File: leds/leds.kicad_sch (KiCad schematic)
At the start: 0 parts

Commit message: first draft
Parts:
- added H1, H2, H3, H4: MountingHole_Pad, MountingHole:MountingHole_4mm_Pad_Via, symbol Mechanical:MountingHole_Pad
- added H5, H6, H7, H8: MountingHole_Pad, MountingHole:MountingHole_3.2mm_M3_Pad_Via, symbol Mechanical:MountingHole_Pad
- added TP10, TP11, TP12, TP13, TP14, TP15, TP16, TP5, TP6, TP7, TP8, TP9: LabeledTestPoint, easyeda2kicad:LabeledTestPoint, symbol easyeda2kicad:LabeledTestPoint
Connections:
- net buckconverter/VIN: now also H1.1, H2.1
- new net GND: H3.1, H4.1, H5.1, H6.1, H7.1, H8.1
- new net a2d/AIN1: TP13.1
- new net a2d/AIN2: TP14.1
- new net a2d/AIN3: TP15.1
- new net a2d/AIN4: TP16.1
- new net esp32/EN1: TP9.1
- new net esp32/EN2: TP10.1
- new net esp32/EN3: TP11.1
- new net esp32/EN4: TP12.1
- new net esp32/LED1: TP5.1
- new net esp32/LED2: TP6.1
- new net esp32/LED3: TP7.1
- new net esp32/LED4: TP8.1
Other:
- added sheet a2d (a2d.kicad_sch)
- added sheet led_channel2 (led_channel.kicad_sch)
- added sheet led_channel3 (led_channel.kicad_sch)
- sheet esp32 ports: added EN1, EN2, EN3, EN4, LED1, LED2, LED3, LED4; removed none
- sheet led_channel ports: added 12V, DEN, DIN, IN, IS; removed none
- sheet led_channel1 ports: added 12V, DEN, DIN, IN, IS; removed none

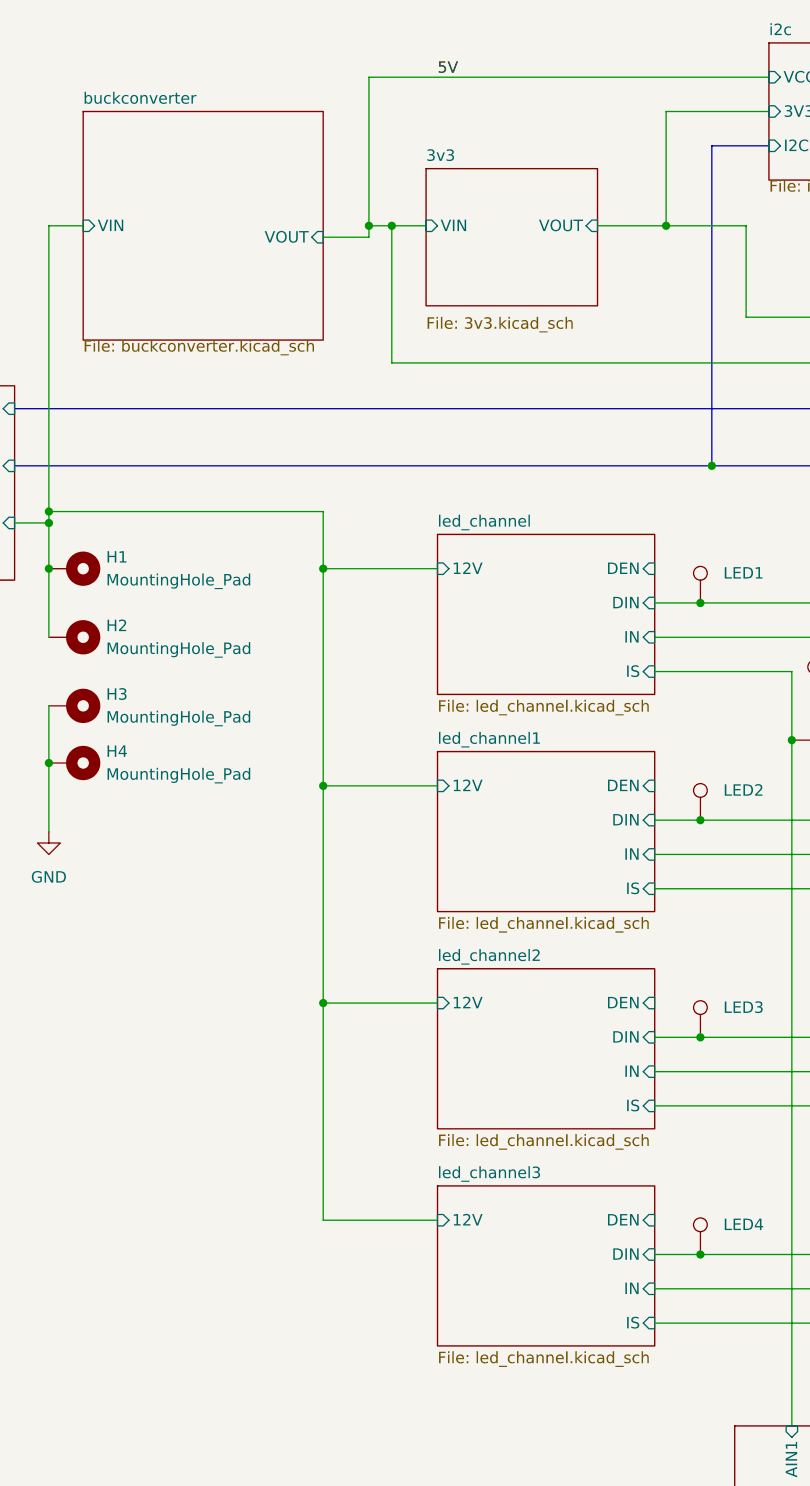
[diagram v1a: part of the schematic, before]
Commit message: Fix errors in LEDs. Revision 0.2 ready to fab.
- [x] Connect VCC on level shifter
- [x] Connect DEN with pull-up
- [x] Add channel on indicator LED - 3.3k
- [x] Flip 3 pin connector
- [x] 82 ohm damping resistor on LED drivers
- [x] Add status LED - white 220 - sinking to ESP
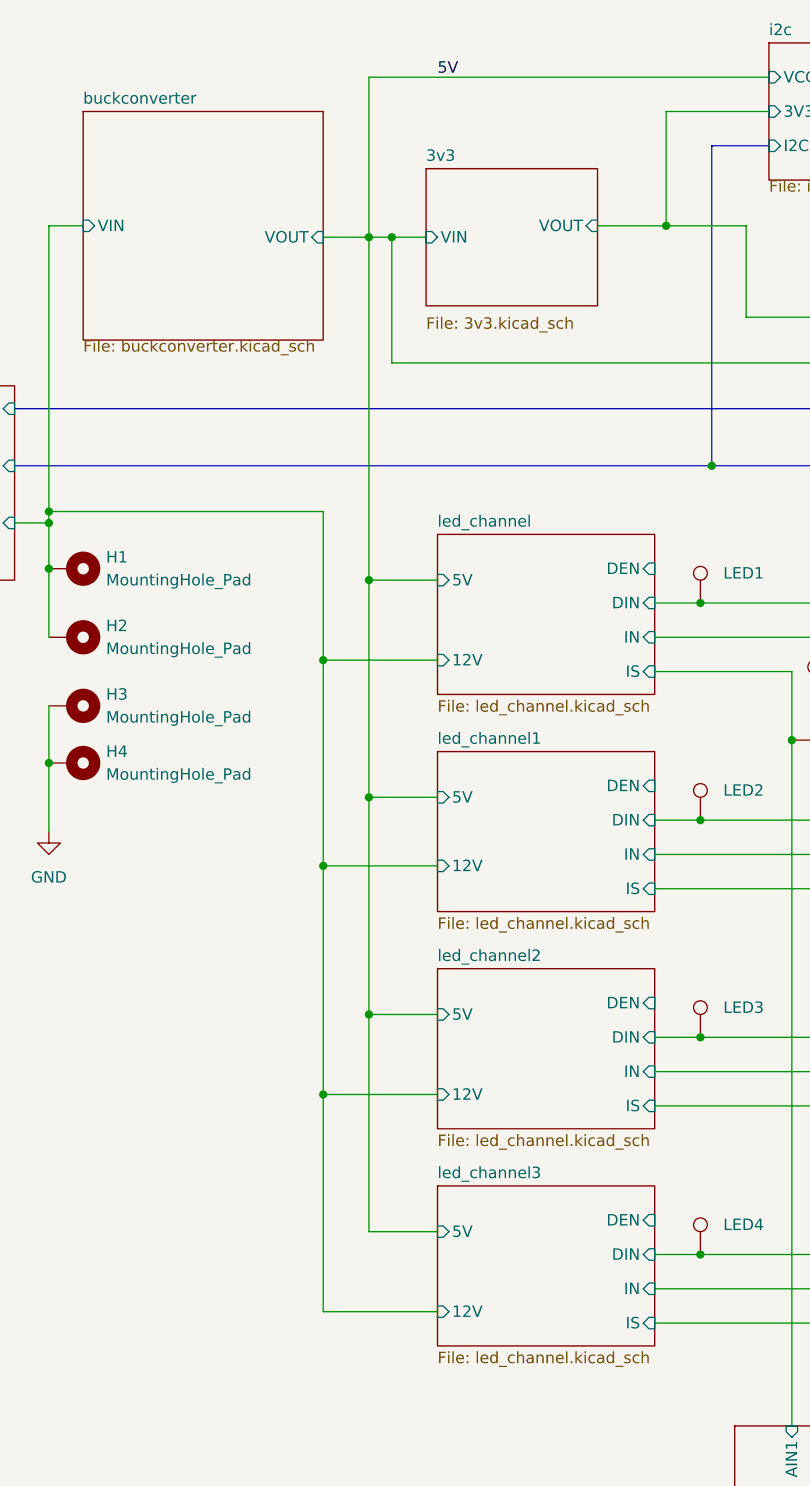
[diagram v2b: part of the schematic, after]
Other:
- sheet led_channel ports: added 5V; removed none
- sheet led_channel1 ports: added 5V; removed none
- sheet led_channel2 ports: added 5V; removed none
- sheet led_channel3 ports: added 5V; removed none
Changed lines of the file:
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@@
 	)
 	(junction
-		(at 139.7 163.83)
+		(at 81.28 100.33)
 		(diameter 0)
 		(color 0 0 0 0)
 	)
 	(junction
-		(at 118.11 102.87)
+		(at 139.7 163.83)
 		(diameter 0)
 		(color 0 0 0 0)
 	)
 	(junction
-		(at 156.21 52.07)
+		(at 118.11 102.87)
 		(diameter 0)
 		(color 0 0 0 0)
 	)
 	(junction
-		(at 118.11 127)
+		(at 156.21 52.07)
 		(diameter 0)
 		(color 0 0 0 0)
 	)
 	(junction
-		(at 76.2 99.06)
+		(at 118.11 127)
 		(diameter 0)
 		(color 0 0 0 0)
@@
 	)
 	(junction
-		(at 76.2 74.93)
+		(at 81.28 124.46)
 		(diameter 0)
 		(color 0 0 0 0)
@@
 	)
 	(junction
-		(at 83.82 36.83)
+		(at 138.43 130.81)
 		(diameter 0)
 		(color 0 0 0 0)
 	)
 	(junction
-		(at 76.2 123.19)
+		(at 114.3 36.83)
 		(diameter 0)
 		(color 0 0 0 0)
 	)
 	(junction
-		(at 81.28 36.83)
+		(at 118.11 78.74)
 		(diameter 0)
 		(color 0 0 0 0)
 	)
 	(junction
-		(at 138.43 130.81)
+		(at 76.2 133.35)
 		(diameter 0)
 		(color 0 0 0 0)
 	)
 	(junction
-		(at 114.3 36.83)
+		(at 128.27 93.98)
 		(diameter 0)
 		(color 0 0 0 0)
 	)
 	(junction
-		(at 118.11 78.74)
+		(at 81.28 76.2)
 		(diameter 0)
 		(color 0 0 0 0)
 	)
 	(junction
-		(at 128.27 93.98)
+		(at 83.82 38.1)
 		(diameter 0)
 		(color 0 0 0 0)
@@
 	)
 	(junction
+		(at 76.2 85.09)
+		(diameter 0)
+		(color 0 0 0 0)
+	)
+	(junction
+		(at 76.2 107.95)
+		(diameter 0)
+		(color 0 0 0 0)
+	)
+	(junction
+		(at 81.28 38.1)
+		(diameter 0)
+		(color 0 0 0 0)
+	)
+	(junction
 		(at 132.08 118.11)
 		(diameter 0)
@@
 	(wire
 		(pts
-			(xy 81.28 20.32) (xy 81.28 36.83)
+			(xy 81.28 20.32) (xy 81.28 38.1)
 		)
 		(stroke
@@
 	(wire
 		(pts
-			(xy 76.2 147.32) (xy 76.2 123.19)
+			(xy 76.2 157.48) (xy 76.2 133.35)
 		)
 		(stroke
@@
 	(wire
 		(pts
-			(xy 76.2 74.93) (xy 76.2 68.58)
+			(xy 76.2 38.1) (xy 81.28 38.1)
 		)
 		(stroke
@@
 	(wire
 		(pts
-			(xy 76.2 38.1) (xy 81.28 38.1)
+			(xy 81.28 100.33) (xy 88.9 100.33)
 		)
 		(stroke
@@
 	(wire
 		(pts
-			(xy 88.9 99.06) (xy 76.2 99.06)
+			(xy 88.9 107.95) (xy 76.2 107.95)
+		)
+		(stroke
+			(width 0)
+			(type default)
+		)
+	)
+	(wire
+		(pts
+			(xy 81.28 76.2) (xy 88.9 76.2)
 		)
 		(stroke
@@
 	(wire
 		(pts
-			(xy 114.3 24.13) (xy 114.3 36.83)
+			(xy 81.28 38.1) (xy 83.82 38.1)
 		)
 		(stroke
@@
 	(wire
 		(pts
-			(xy 113.03 86.36) (xy 128.27 86.36)
+			(xy 114.3 24.13) (xy 114.3 36.83)
 		)
 		(stroke
@@
 	(wire
 		(pts
-			(xy 76.2 99.06) (xy 76.2 74.93)
+			(xy 113.03 86.36) (xy 128.27 86.36)
 		)
 		(stroke
@@
 	(wire
 		(pts
-			(xy 88.9 74.93) (xy 76.2 74.93)
+			(xy 88.9 85.09) (xy 76.2 85.09)
+		)
+		(stroke
+			(width 0)
+			(type default)
+		)
+	)
+	(wire
+		(pts
+			(xy 81.28 148.59) (xy 81.28 124.46)
 		)
 		(stroke
@@
 	(wire
 		(pts
+			(xy 81.28 100.33) (xy 81.28 76.2)
+		)
+		(stroke
+			(width 0)
+			(type default)
+		)
+	)
+	(wire
+		(pts
 			(xy 132.08 170.18) (xy 132.08 118.11)
 		)
@@
 	(wire
 		(pts
+			(xy 81.28 76.2) (xy 81.28 38.1)
+		)
+		(stroke
+			(width 0)
+			(type default)
+		)
+	)
+	(wire
+		(pts
 			(xy 113.03 78.74) (xy 118.11 78.74)
 		)
@@
 	(wire
 		(pts
-			(xy 198.12 27.94) (xy 210.82 27.94)
+			(xy 76.2 68.58) (xy 76.2 85.09)
 		)
 		(stroke
@@
 	(wire
 		(pts
-			(xy 88.9 147.32) (xy 76.2 147.32)
+			(xy 198.12 27.94) (xy 210.82 27.94)
 		)
 		(stroke
@@
 	(wire
 		(pts
-			(xy 45.72 68.58) (xy 45.72 69.85)
+			(xy 88.9 157.48) (xy 76.2 157.48)
 		)
 		(stroke
@@
 	(wire
 		(pts
-			(xy 81.28 38.1) (xy 81.28 36.83)
+			(xy 45.72 68.58) (xy 45.72 69.85)
 		)
 		(stroke
@@
 	(wire
 		(pts
-			(xy 138.43 130.81) (xy 167.64 130.81)
+			(xy 76.2 107.95) (xy 76.2 133.35)
 		)
 		(stroke
@@
 	(wire
 		(pts
-			(xy 210.82 27.94) (xy 220.98 27.94)
+			(xy 88.9 148.59) (xy 81.28 148.59)
 		)
 		(stroke
@@
 	(wire
 		(pts
-			(xy 88.9 123.19) (xy 76.2 123.19)
+			(xy 138.43 130.81) (xy 167.64 130.81)
+		)
+		(stroke
+			(width 0)
+			(type default)
+		)
+	)
+	(wire
+		(pts
+			(xy 210.82 27.94) (xy 220.98 27.94)
 		)
 		(stroke
@@
 	(wire
 		(pts
-			(xy 81.28 36.83) (xy 83.82 36.83)
+			(xy 88.9 133.35) (xy 76.2 133.35)
 		)
 		(stroke
@@
 	(wire
 		(pts
+			(xy 81.28 124.46) (xy 81.28 100.33)
+		)
+		(stroke
+			(width 0)
+			(type default)
+		)
+	)
+	(wire
+		(pts
 			(xy 118.11 102.87) (xy 167.64 102.87)
 		)
@@
 		)
 	)
+	(wire
+		(pts
+			(xy 81.28 124.46) (xy 88.9 124.46)
+		)
+		(stroke
+			(width 0)
+			(type default)
+		)
+	)
 	(bus
 		(pts
@@
 	(wire
 		(pts
-			(xy 83.82 52.07) (xy 83.82 36.83)
+			(xy 83.82 52.07) (xy 83.82 38.1)
 		)
 		(stroke
@@
 	(wire
 		(pts
-			(xy 76.2 123.19) (xy 76.2 99.06)
+			(xy 76.2 85.09) (xy 76.2 107.95)
 		)
 		(stroke
@@
 	(wire
 		(pts
-			(xy 83.82 36.83) (xy 87.63 36.83)
+			(xy 83.82 38.1) (xy 87.63 38.1)
 		)
 		(stroke
@@
 		)
 		(pin "12V" input
-			(at 88.9 99.06 180)
+			(at 88.9 107.95 180)
 			(effects
 				(font
@@
 			)
 		)
+		(pin "5V" input
+			(at 88.9 100.33 180)
+			(effects
+				(font
+					(size 1.27 1.27)
+				)
+				(justify left)
+			)
+		)
 		(instances
 			(project "leds"
@@
 		)
 		(pin "12V" input
-			(at 88.9 147.32 180)
+			(at 88.9 157.48 180)
 			(effects
 				(font
@@
 			)
 		)
+		(pin "5V" input
+			(at 88.9 148.59 180)
+			(effects
+				(font
+					(size 1.27 1.27)
+				)
+				(justify left)
+			)
+		)
 		(instances
 			(project "leds"
@@
 		)
 		(pin "12V" input
-			(at 88.9 123.19 180)
+			(at 88.9 133.35 180)
 			(effects
 				(font
@@
 			)
 		)
+		(pin "5V" input
+			(at 88.9 124.46 180)
+			(effects
+				(font
+					(size 1.27 1.27)
+				)
+				(justify left)
+			)
+		)
 		(instances
 			(project "leds"
@@
 		)
 		(pin "12V" input
-			(at 88.9 74.93 180)
+			(at 88.9 85.09 180)
 			(effects
 				(font
@@
 			)
 		)
+		(pin "5V" input
+			(at 88.9 76.2 180)
+			(effects
+				(font
+					(size 1.27 1.27)
+				)
+				(justify left)
+			)
+		)
 		(instances
 			(project "leds"
@@
 		)
 		(pin "VIN" input
-			(at 87.63 36.83 180)
+			(at 87.63 38.1 180)
 			(effects
 				(font
